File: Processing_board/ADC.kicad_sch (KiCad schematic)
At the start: 36 parts, among them U2 OPA192IDR, U3 REF5025AQDRQ1, U4 ADS7953SBDBT

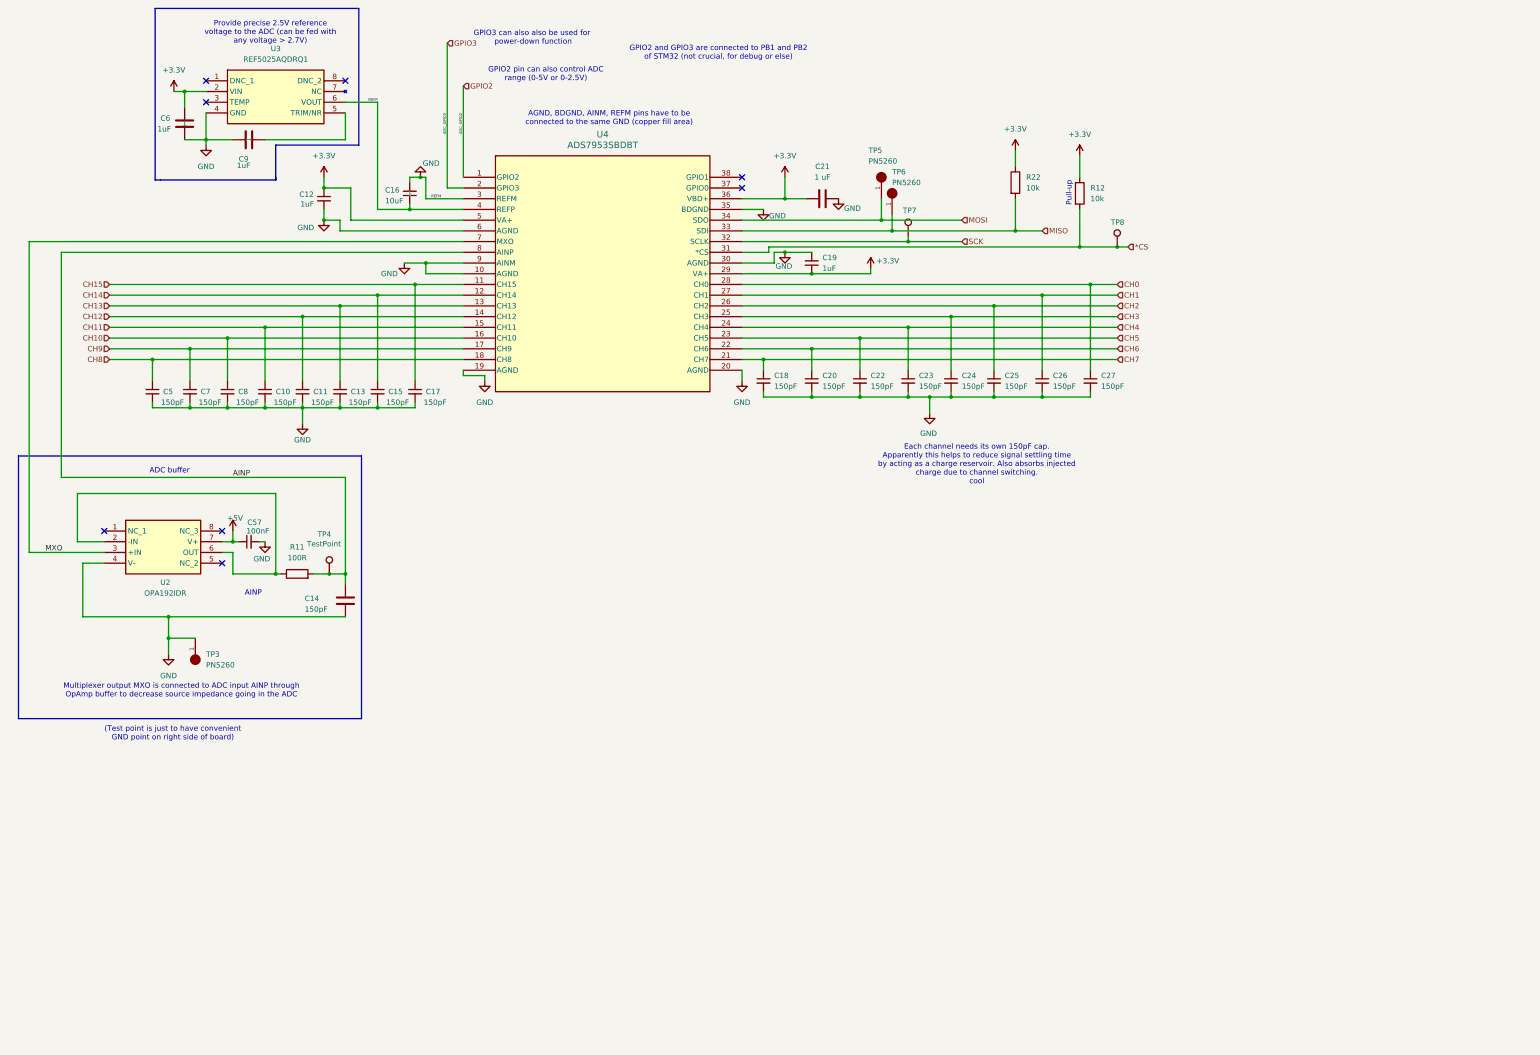
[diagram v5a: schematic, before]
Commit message: feat: connected GNDA, VDDA, active electrodes and REF.
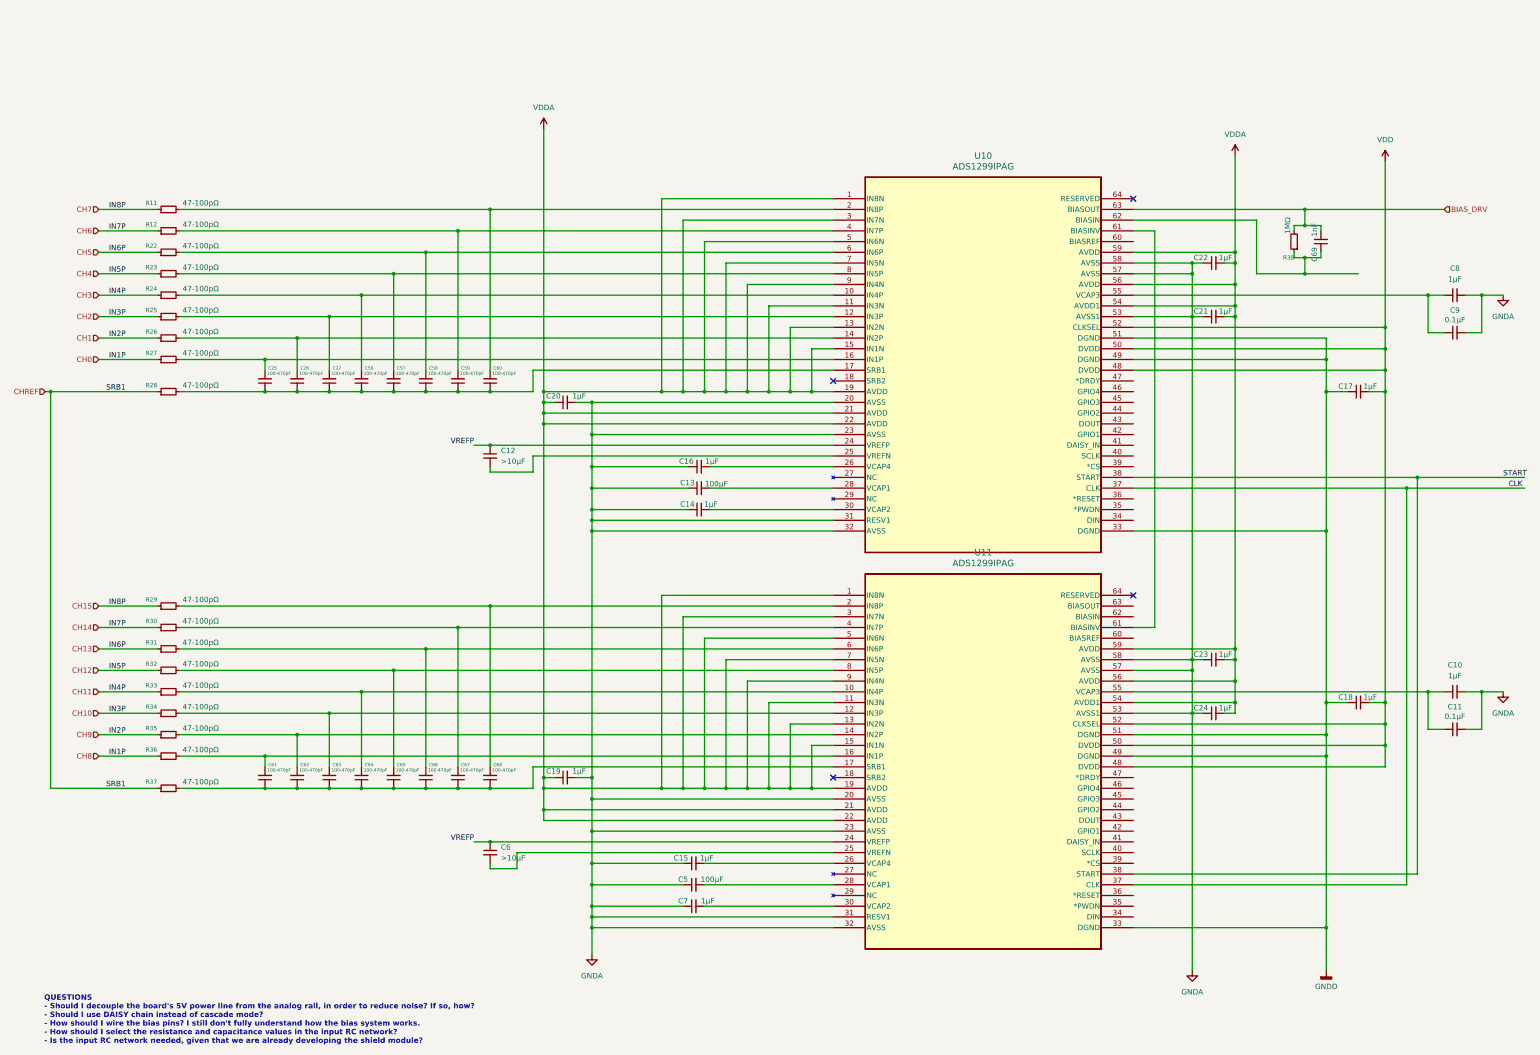
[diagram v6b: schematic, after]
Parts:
- removed C14: 150pF, Capacitor_SMD:C_0402_1005Metric, symbol Device:C
- removed C21: 1 uF, Capacitor_SMD:C_0402_1005Metric, symbol Device:C
- removed C6, C9: 1uF, Capacitor_SMD:C_0402_1005Metric, symbol Device:C
- removed R11: 100R, Resistor_SMD:R_0402_1005Metric, symbol Device:R
- removed R12, R22: 10k, Resistor_SMD:R_0402_1005Metric, symbol Device:R
- removed TP3, TP5, TP6: PN5260, PN5260:PN5260, symbol PN5260:5260
- removed TP4, TP7, TP8: TestPoint, TestPoint:TestPoint_Pad_D1.0mm, symbol Connector:TestPoint
- removed U2: OPA192IDR, OPA192IDR:SOIC127P600X175-8N, symbol OPA192IDR:OPA192IDR
- removed U3: REF5025AQDRQ1, REF5025AQDRQ1:SOIC127P600X175-8N, symbol REF5025AQDRQ1:REF5025AQDRQ1
- removed U4: ADS7953SBDBT, ADS7953SBDBT:DBT38, symbol 2025-03-12_09-53-19:ADS7953SBDBT
- added C14, C21: 1μF, symbol Device:C_Small
- added C56, C58, C59, C60, C61, C62, C63, C64, C65, C66, C67, C68: 100-470pF, symbol Device:C_Small
- added C6: >10μF, symbol Device:C_Small
- added C69: 1nF, symbol Device:C_Small
- added C9: 0.1μF, symbol Device:C_Small
- added R11, R12, R22, R23, R24, R25, R26, R27, R28, R29, R30, R31, R32, R33, R34, R35, R36, R37: 47-100pΩ, symbol Device:R_Small
- added R38: 1MΩ, symbol Device:R_Small
- added U10, U11: ADS1299IPAG, PAG64_TEX, symbol ADS1299:ADS1299IPAG
- C10, C15, C17, C18, C20, C22, C23, C24, C7, C8: value 150pF -> 1μF; footprint Capacitor_SMD:C_0402_1005Metric -> (none); Link https://www.mouser.ch/ProductDetail/KEMET/C0402C151K5RACTU?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 -> (none); MANUFACTURER KEMET -> (none); Manufacturer_Part_Number C0402C151K5RACTU -> (none); Panier 1 -> (none)
- C11: value 150pF -> 0.1μF; footprint Capacitor_SMD:C_0402_1005Metric -> (none); Link https://www.mouser.ch/ProductDetail/KEMET/C0402C151K5RACTU?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 -> (none); MANUFACTURER KEMET -> (none); Manufacturer_Part_Number C0402C151K5RACTU -> (none); Panier 1 -> (none)
- C12: value 1uF -> >10μF; footprint Capacitor_SMD:C_0402_1005Metric -> (none); Link https://www.mouser.ch/ProductDetail/Samsung-Electro-Mechani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 -> (none); MANUFACTURER Samsung Electro-Mechanics -> (none); Manufacturer_Part_Number CL05A105KP5NNNC -> (none); Panier 1 -> (none)
- C13, C5: value 150pF -> 100μF; footprint Capacitor_SMD:C_0402_1005Metric -> (none); Link https://www.mouser.ch/ProductDetail/KEMET/C0402C151K5RACTU?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 -> (none); MANUFACTURER KEMET -> (none); Manufacturer_Part_Number C0402C151K5RACTU -> (none); Panier 1 -> (none)
- C16: value 10uF -> 1μF; footprint Capacitor_SMD:C_0402_1005Metric -> (none); Link https://www.mouser.ch/ProductDetail/Murata-Electronics/GRM1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 -> (none); MANUFACTURER Murata Electronics -> (none); Manufacturer_Part_Number GRM155R61A106ME11D -> (none); Panier 1 -> (none)
- C19: value 1uF -> 1μF; footprint Capacitor_SMD:C_0402_1005Metric -> (none); Link https://www.mouser.ch/ProductDetail/Samsung-Electro-Mechani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 -> (none); MANUFACTURER Samsung Electro-Mechanics -> (none); Manufacturer_Part_Number CL05A105KP5NNNC -> (none); Panier 1 -> (none)
- C25, C26, C27: value 150pF -> 100-470pF; footprint Capacitor_SMD:C_0402_1005Metric -> (none); Link https://www.mouser.ch/ProductDetail/KEMET/C0402C151K5RACTU?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 -> (none); MANUFACTURER KEMET -> (none); Manufacturer_Part_Number C0402C151K5RACTU -> (none); Panier 1 -> (none)
- C57: value 100nF -> 100-470pF; footprint Capacitor_SMD:C_0402_1005Metric -> (none); Link https://eu.mouser.com/ProductDetail/Samsung-Electro-Mechani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 -> (none); MANUFACTURER Samsung Electro-Mechanics -> (none); Manufacturer_Part_Number CL05B104KP5VPNC -> (none); Panier 1 -> (none)
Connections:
- net CH2 is gone; now on an unnamed net: C25.1
- net CH4 is gone; now on net GNDA: C23.1
- net CH5 is gone; now on net GNDA: C22.1
- net CH6 is gone; now on net VDDA: C20.1
- net CH8 is gone; now on net GNDA: C5.1
- net CH9 is gone; now on net GNDA: C7.1
- net REFP is gone; now on net GNDA: C16.1
- net CH0: now also R27.1, R36.1; no longer C27.1
- net CH1: now also R26.1, R35.1; no longer C26.1
- net CH10: now also R25.1, R34.1; no longer C8.1
- net CH11: now also R24.1, R33.1; no longer C10.1
- net CH12: now also R23.1, R32.1; no longer C11.1
- net CH13: now also R22.1, R31.1; no longer C13.1
- net CH14: now also R12.1, R30.1; no longer C15.1
- net CH15: now also R11.1, R29.1; no longer C17.1
- net +3.3V renamed VDDA
- net VDDA: now also C22.2, C23.2, C24.2, C21.2, U10.1 (IN8N), U10.11 (IN3N), U10.13 (IN2N), U10.15 (IN1N), U10.19 (AVDD), U10.21 (AVDD), U10.22 (AVDD), U10.3 (IN7N), U10.5 (IN6N), U10.54 (AVDD1), U10.56 (AVDD), U10.59 (AVDD), U10.7 (IN5N), U10.9 (IN4N), U11.1 (IN8N), U11.11 (IN3N), U11.13 (IN2N), U11.15 (IN1N), U11.19 (AVDD), U11.21 (AVDD), U11.22 (AVDD), U11.3 (IN7N), U11.5 (IN6N), U11.54 (AVDD1), U11.56 (AVDD), U11.59 (AVDD), U11.7 (IN5N), U11.9 (IN4N); no longer C12.1
- net +5V: no longer names the net of C57.1
- net +5V: now also C26.1, C27.1, C56.1, C58.1, C59.1, C60.1, R28.2, U10.17 (SRB1)
- net CH3 renamed GNDA
- net GNDA: now also C10.2, C11.2, C13.1, C15.1, C19.2, C20.2, C8.2, C14.1, C21.1, C9.2, U10.20 (AVSS), U10.23 (AVSS), U10.31 (RESV1), U10.32 (AVSS), U10.53 (AVSS1), U10.57 (AVSS), U10.58 (AVSS), U11.20 (AVSS), U11.23 (AVSS), U11.31 (RESV1), U11.32 (AVSS), U11.53 (AVSS1), U11.57 (AVSS), U11.58 (AVSS)
- net CH7 renamed GNDD
- net GNDD: now also C17.1, U10.33 (DGND), U10.49 (DGND), U10.51 (DGND), U11.33 (DGND), U11.49 (DGND), U11.51 (DGND)
- removed net GND: C10.2, C11.2, C12.2, C13.2, C15.2, C16.2, C17.2, C18.2, C19.2, C20.2, C22.2, C23.2, C24.2, C25.2, C26.2, C27.2, C5.2, C57.2, C7.2, C8.2
- new net: C10.1, C11.1, U11.55 (VCAP3)
- new net: C6.2, U11.25 (VREFN)
- new net: C27.2, R25.2, U10.12 (IN3P)
- new net: C61.1, C62.1, C63.1, C64.1, C65.1, C66.1, C67.1, C68.1, R37.2, U11.17 (SRB1)
- new net: C68.2, R29.2, U11.2 (IN8P)
- new net: C65.2, R32.2, U11.8 (IN5P)
- new net: C13.2, U10.28 (VCAP1)
- new net: C64.2, R33.2, U11.10 (IN4P)
- new net: C56.2, R24.2, U10.10 (IN4P)
- new net: C26.2, R26.2, U10.14 (IN2P)
- new net: C25.2, R27.2, U10.16 (IN1P)
- new net: C60.2, R11.2, U10.2 (IN8P)
- new net: C12.2, U10.25 (VREFN)
- new net: C16.2, U10.26 (VCAP4)
- new net: C14.2, U10.30 (VCAP2)
- new net: C59.2, R12.2, U10.4 (IN7P)
- new net: C8.1, C9.1, U10.55 (VCAP3)
- new net: C58.2, R22.2, U10.6 (IN6P)
- new net: U10.61 (BIASINV), U11.61 (BIASINV)
- new net: C69.1, R38.1, U10.62 (BIASIN)
- new net: C57.2, R23.2, U10.8 (IN5P)
- new net: C7.2, U11.30 (VCAP2)
- new net: C61.2, R36.2, U11.16 (IN1P)
- new net: C67.2, R30.2, U11.4 (IN7P)
- new net: C5.2, U11.28 (VCAP1)
- new net: C66.2, R31.2, U11.6 (IN6P)
- new net: C63.2, R34.2, U11.12 (IN3P)
- new net: C62.2, R35.2, U11.14 (IN2P)
- new net: C15.2, U11.26 (VCAP4)
- new net BIAS_DRV: C69.2, R38.2, U10.63 (BIASOUT)
- new net CHREF: R28.1, R37.1
- new net CLK: U10.37 (CLK), U11.37 (CLK)
- new net START: U10.38 (START), U11.38 (START)
- new net VDD: C17.2, C18.2, U10.48 (DVDD), U10.50 (DVDD), U10.52 (CLKSEL), U11.48 (DVDD), U11.50 (DVDD), U11.52 (CLKSEL)
- new net VREFP: C12.1, C6.1, U10.24 (VREFP), U11.24 (VREFP)
- no-connect marks 8 -> 4
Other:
- note added: "QUESTIONS - Should I decouple the board's 5V power line from the analog rail, in order to reduce noise? If so, how? - Should I use DAISY chain instead of cascade mode? - How should I wire the bias pins? I still don't fully understand how the bias system works. - How should I select the resistance and capacitance values in the input RC network? - Is the input RC network needed, given that we are a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"
- note removed: "(Test point is just to have convenient GND point on right side of board)"
- note removed: "ADC buffer"
- note removed: "AGND, BDGND, AINM, REFM pins have to be connected to the same GND (copper fill area)"
- note removed: "AINP"
- note removed: "Each channel needs its own 150pF cap. Apparently this helps to reduce signal settling time by acting as a charge reservoir. Also absorbs injected charge due to channel switching. cool"
- note removed: "GPIO2 and GPIO3 are connected to PB1 and PB2 of STM32 (not crucial, for debug or else)"
- note removed: "GPIO2 pin can also control ADC range (0-5V or 0-2.5V)"
- note removed: "GPIO3 can also also be used for power-down function"
- note removed: "Multiplexer output MXO is connected to ADC input AINP through OpAmp buffer to decrease source impedance going in the ADC"
- note removed: "Provide precise 2.5V reference voltage to the ADC (can be fed with any voltage > 2.7V)"
- note removed: "Pull-up"
